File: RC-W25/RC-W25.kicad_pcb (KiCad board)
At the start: 2 copper layers, 36 x 100.1 mm, 55 parts, among them J1 USB_C_Receptacle_USB2.0_14P, P1 JST CONN, P2 JST CONN, Q1 NMOS, SW1 Button, SW2 Button, SW3 YTSPS-22E58LM, SW4 Button, U1 ESP32-C6-MINI-1, U2 MCP73831-5-OT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

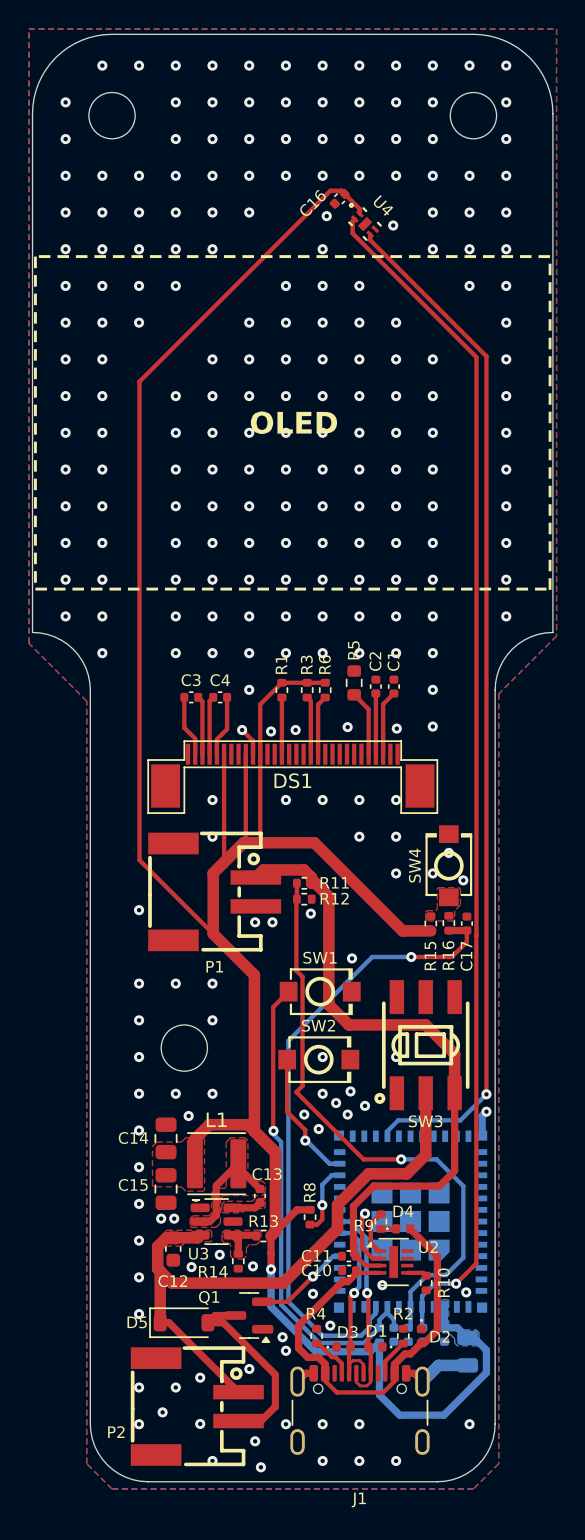
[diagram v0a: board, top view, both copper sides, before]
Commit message: crc v2
main board and receiver finalized. ready for assembly!
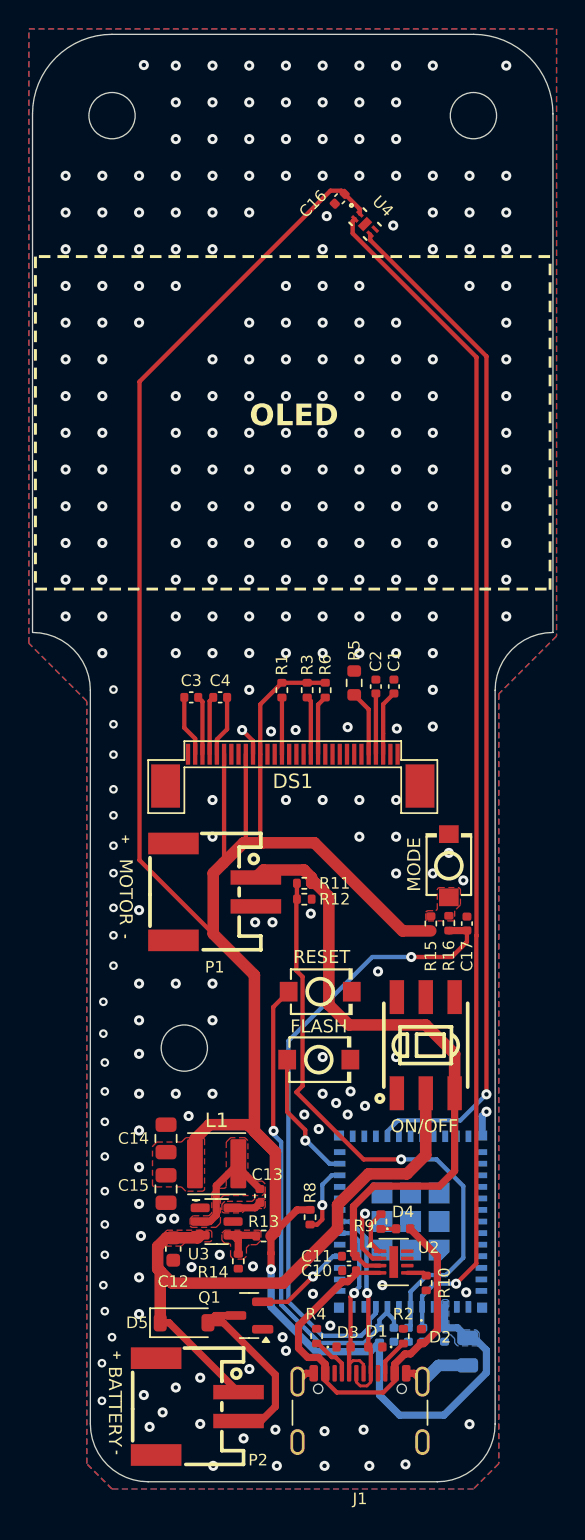
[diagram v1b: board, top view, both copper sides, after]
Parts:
- added G***: LOGO, LOGO, B.Cu at (113.5, 105.7)
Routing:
- net GND: vias 259 -> 275
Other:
- board text added: "+"
- board text added: "-"
- board text added: "BATTERY"
- board text added: "FLASH"
- board text added: "MATTHEW EMBAYE"
- board text added: "MODE"
- board text added: "MOTOR"
- board text added: "ON/OFF"
- board text added: "RESET"

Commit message: crc v2
remote and receiver complete! assembly and orders have been prepared for purchasing.
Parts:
- D1, D2, D3, D4: footprint Diode_SMD:D_0402_1005Metric -> footprints:D_0402_1005Metric
- R11: value 42k -> 300
- R12: value 10k -> 1.1k
- R13: value 33.2k -> 31.6k
- R2, R4: value 5.7k -> 5.1k
- U3: value AP62300TWU -> AP62300Z6; footprint Package_TO_SOT_SMD:TSOT-23-6 -> Package_TO_SOT_SMD:SOT-563
- moved R14 7.33 mm to (119.6, 102.6), turned to 180 degrees
- moved C14 6.05 mm to (116.0, 107.3)
- moved C12 4.83 mm to (116.2, 104.1)
- moved R13 4.74 mm to (121.5, 103.5)
- moved L1 4.32 mm to (119.3, 107.3)
- moved C15 3.39 mm to (114.0, 107.3), turned to 90 degrees
- moved U3 2.93 mm to (119.3, 104.1)
- moved C13 1.43 mm to (121.5, 104.5), turned to 180 degrees
- renumbered R8 to R7, R7 to R8
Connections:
- U3 pad 1: GND -> +VBAT
- U3 pad 3: +VBAT -> GND
- U3 pad 4: Net-(U3-FB) -> Net-(U3-BST)
- U3 pad 6: Net-(U3-BST) -> Net-(U3-FB)
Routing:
- net +3.3V: track 181.1 -> 193.8 mm
- net +VBAT: track 43.9 -> 54.2 mm
- net Net-(U3-FB): track 3.06 -> 1.26 mm
- net GPIO_EN1: track 71.1 -> 72.4 mm
- net Net-(U3-BST): track 2.00 -> 1.10 mm
- net ADC_HALLEFFECT1: track 82.8 -> 81.9 mm
- net GND: track 14.4 -> 13.8 mm, vias 275 -> 285
- removed copper zone on F.Cu, net +3.3V
- removed copper zone on F.Cu, net +VBAT
- removed copper zone on F.Cu, net Net-(U3-BST)

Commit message: Custom RC V2
Final Remote + Receiver!

Special thanks to the CRCW25 Electrical Team who contributed to its development!

Jun
Katie
Nelson
David
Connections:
- U1 pad 13: unconnected-(U1-IO1-Pad13) -> GPIO_RUMBLE_CNTL
- U1 pad 15: GPIO_RUMBLE_CNTL -> SDA_DISPLAY
- U1 pad 16: unconnected-(U1-IO7-Pad16) -> SCL_DISPLAY
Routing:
- net SDA_DISPLAY: track 4.03 -> 44.6 mm, vias 0 -> 1
- net SCL_DISPLAY: track 4.13 -> 43.3 mm, vias 0 -> 1
- net GPIO_MODE: track 43.7 -> 45.0 mm
- net GPIO_RUMBLE_CNTL: track 6.63 -> 5.97 mm
